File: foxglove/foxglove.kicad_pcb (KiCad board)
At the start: 4 copper layers, 70.7 x 53.3 mm, 106 parts, among them IC1 LFE5U-12F-6BG256C, J1 NEIGHBOR1, J2 NEIGHBOR2, J3 Conn_02x05_Odd_Even, J4 Conn_02x05_Odd_Even, J5 Conn_01x02_Female, J7 BONUS_ROW, U1 ICE40HX8K-CT256, U10 SHIFTER, U11 74HC4051, U12 SHIFTER, U13 74HC4051, U14 SHIFTER, U15 74HC4051, U16 SHIFTER, U17 74HC4051, U18 SHIFTER, U19 74HC4051, U2 ADP225, U20 SHIFTER, U21 74HC4051, U22 SHIFTER, U23 74HC4051, U24 SHIFTER, U3 MC4558CPT, U4 74LVC1G3157, U5 LM339, U6 ADP225, U7 DAC084S085, U8 74AHC1G04, U9 74HC4051

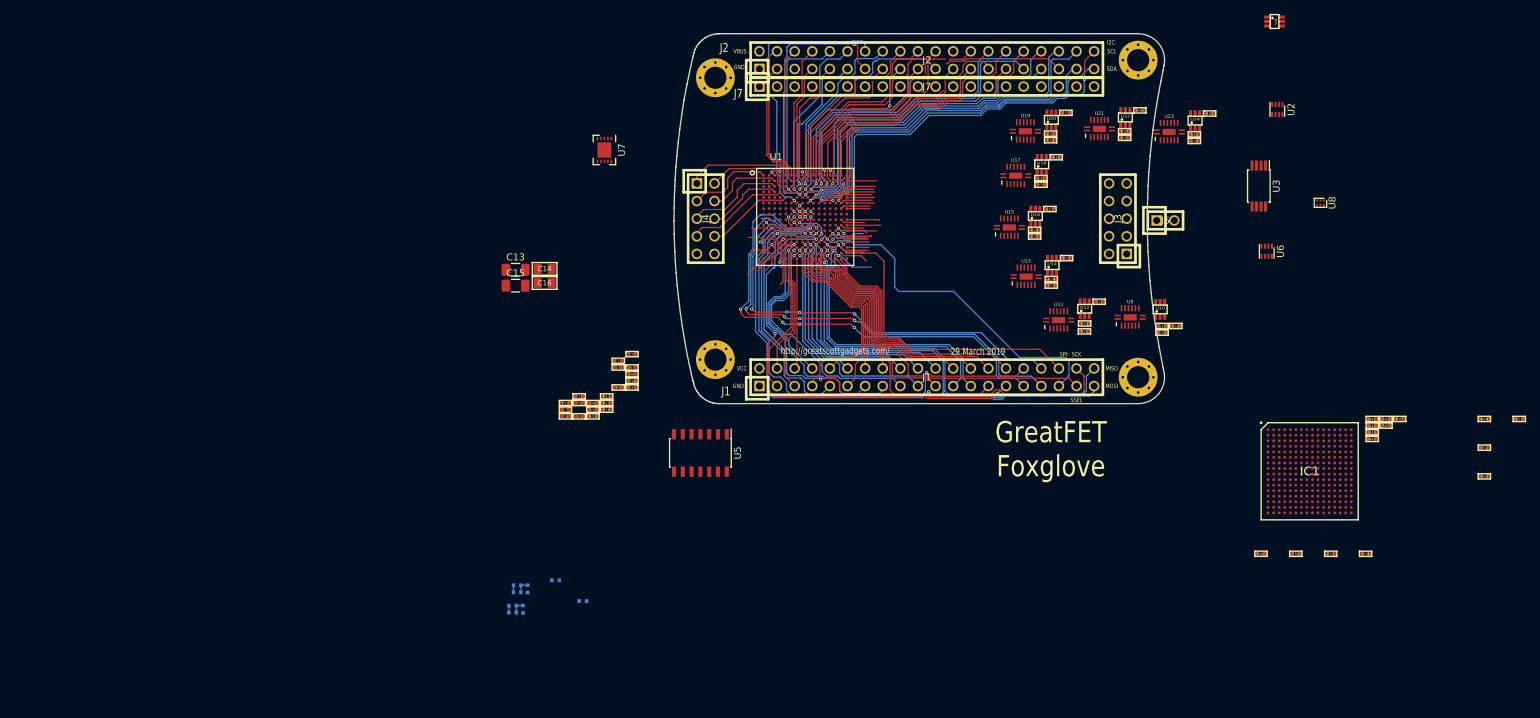
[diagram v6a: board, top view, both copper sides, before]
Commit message: Started routing connections to J2 and J7
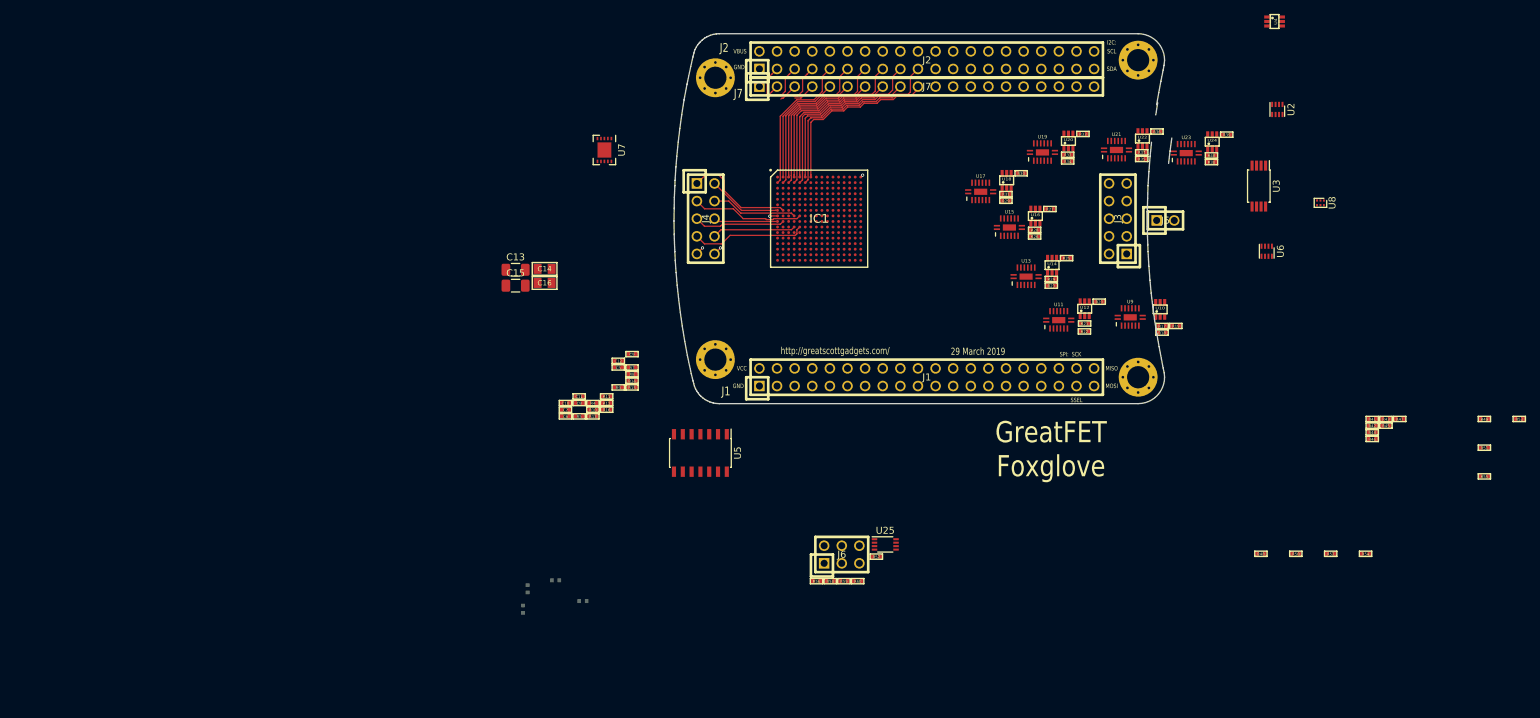
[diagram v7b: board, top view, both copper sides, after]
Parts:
- removed C1, C3: 10uF, gsg-modules:0402
- removed C2, C4: 100nF, gsg-modules:0402
- removed U1: ICE40HX8K-CT256, gsg-modules:BGA256C80P16X16_1400X1400X170
- added J6: Conn_02x03_Odd_Even, gsg-modules:HEADER-2x3, F.Cu at (133.8, 143.7)
- added R56: 4.7k, gsg-modules:0402, F.Cu at (130.1, 147.5)
- added R57: 4.7k, gsg-modules:0402, F.Cu at (138.8, 144.0)
- added R58: 1k, gsg-modules:0402, F.Cu at (132.1, 147.5)
- added R59: 4.7k, gsg-modules:0402, F.Cu at (134.1, 147.5)
- added R60: 4.7k, gsg-modules:0402, F.Cu at (136.1, 147.5)
- added U25: 74LVC1G53, Package_SO:VSSOP-8_2.3x2mm_P0.5mm, F.Cu at (140.1, 142.2)
- R1, R4, R5: value 10k -> 4.7k
- R2: value ??? -> 4.7k
- R3, R6: value 100 -> 4.7k
- moved IC1 79.6 mm to (130.5, 95.2)
- moved R30 5.56 mm to (159.7, 88.7)
- moved R31 5.56 mm to (157.5, 91.7)
- moved U18 5.56 mm to (157.6, 89.7)
- moved R29 5.56 mm to (157.5, 92.7)
- moved U17 5.56 mm to (153.8, 91.4)
- moved U21 3.92 mm to (173.4, 85.3)
- moved U22 3.92 mm to (177.2, 83.7)
- moved R32 3.92 mm to (166.4, 86.0)
- moved R33 3.92 mm to (168.6, 83.0)
- moved R35 3.92 mm to (177.0, 86.6)
- moved R36 3.92 mm to (179.2, 82.7)
- moved R37 3.92 mm to (177.0, 85.7)
- moved R38 3.92 mm to (187.1, 87.1)
- moved R39 3.92 mm to (189.3, 83.1)
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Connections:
- IC1 pad A10: (no net) -> /J7.13
- IC1 pad A11: (no net) -> /J7.14
- IC1 pad A12: (no net) -> /J7.15
- IC1 pad A13: (no net) -> /J7.16
- IC1 pad A14: (no net) -> /J7.17
- IC1 pad A15: (no net) -> /J7.18
- IC1 pad A2: (no net) -> /J7.05
- IC1 pad A3: (no net) -> /J7.06
- IC1 pad A4: (no net) -> /J7.07
- IC1 pad A5: (no net) -> /J7.08
- IC1 pad A6: (no net) -> /J7.09
- IC1 pad A7: (no net) -> /J7.10
- IC1 pad A8: (no net) -> /J7.11
- IC1 pad A9: (no net) -> /J7.12
- IC1 pad B1: (no net) -> /J2.09
- IC1 pad B10: (no net) -> /J2.27
- IC1 pad B11: (no net) -> /J2.29
- IC1 pad B12: (no net) -> /J2.31
- IC1 pad B13: (no net) -> /J2.33
- IC1 pad B14: (no net) -> /J2.35
- IC1 pad B15: (no net) -> /J2.37
- IC1 pad B16: (no net) -> /J2.39
- IC1 pad B2: (no net) -> /J2.11
- IC1 pad B3: (no net) -> /J2.13
- IC1 pad B4: (no net) -> /J2.15
- IC1 pad B5: (no net) -> /J2.17
- IC1 pad B6: (no net) -> /J2.19
- IC1 pad B7: (no net) -> /J2.21
- IC1 pad B8: (no net) -> /J2.23
- IC1 pad B9: (no net) -> /J2.25
- IC1 pad C1: (no net) -> /J2.10
- IC1 pad C10: (no net) -> /J2.28
- IC1 pad C11: (no net) -> /J2.30
- IC1 pad C12: (no net) -> /J2.32
- IC1 pad C13: (no net) -> /J2.34
- IC1 pad C14: (no net) -> /J2.36
- IC1 pad C15: (no net) -> /J2.38
- IC1 pad C16: (no net) -> /J2.40
- IC1 pad C2: (no net) -> /J2.12
- IC1 pad C3: (no net) -> /J2.14
- IC1 pad C4: (no net) -> /J2.16
- IC1 pad C5: (no net) -> /J2.18
- IC1 pad C6: (no net) -> /J2.20
- IC1 pad C7: (no net) -> /J2.22
- IC1 pad C8: (no net) -> /J2.24
- IC1 pad C9: (no net) -> /J2.26
- IC1 pad G1: (no net) -> /B2
- IC1 pad G2: (no net) -> /B1
- IC1 pad H4: (no net) -> /B4
- IC1 pad H5: (no net) -> /B3
- IC1 pad J1: (no net) -> /B6
- IC1 pad J2: (no net) -> /B5
- IC1 pad K4: (no net) -> /B8
- IC1 pad K5: (no net) -> /B7
- IC1 pad L6: (no net) -> VCC
- IC1 pad M10: (no net) -> /TDO
- IC1 pad N10: (no net) -> /CFG_0
- IC1 pad N8: (no net) -> /CSSPIN
- IC1 pad N9: (no net) -> /SCK
- IC1 pad P10: (no net) -> /CFG_1
- IC1 pad R1: (no net) -> /J1.13
- IC1 pad R10: (no net) -> /CFG_2
- IC1 pad R11: (no net) -> /TDI
- IC1 pad R12: (no net) -> /J1.27
- IC1 pad R13: (no net) -> /J1.29
- IC1 pad R14: (no net) -> /J1.31
- IC1 pad R15: (no net) -> /J1.33
- IC1 pad R16: (no net) -> /J1.35
- IC1 pad R2: (no net) -> /J1.15
- IC1 pad R3: (no net) -> /J1.17
- IC1 pad R4: (no net) -> /J1.19
- IC1 pad R5: (no net) -> /J1.21
- IC1 pad R6: (no net) -> /J1.23
- IC1 pad R7: (no net) -> /J1.25
- IC1 pad R8: (no net) -> /SSEL
- IC1 pad R9: (no net) -> /PROGRAMN
- IC1 pad T10: (no net) -> /TCK
- IC1 pad T11: (no net) -> /TMS
- IC1 pad T13: (no net) -> /J1.32
- IC1 pad T14: (no net) -> /J1.34
- IC1 pad T15: (no net) -> /J1.36
- IC1 pad T2: (no net) -> /J1.24
- IC1 pad T3: (no net) -> /J1.26
- IC1 pad T4: (no net) -> /J1.28
- IC1 pad T6: (no net) -> /J1.30
- IC1 pad T7: (no net) -> /MISO
- IC1 pad T8: (no net) -> /MOSI
- IC1 pad T9: (no net) -> /INITN
- J1 pad 10: /J1.10 -> (no net)
- J1 pad 11: /J1.11 -> (no net)
- J1 pad 12: /J1.12 -> (no net)
- J1 pad 14: /J1.14 -> (no net)
- J1 pad 16: /J1.16 -> (no net)
- J1 pad 18: /J1.18 -> (no net)
- J1 pad 20: /J1.20 -> (no net)
- J1 pad 22: /J1.22 -> (no net)
- J1 pad 3: /J1.03 -> (no net)
- J1 pad 4: /J1.04 -> (no net)
- J1 pad 5: /J1.05 -> (no net)
- J1 pad 6: /J1.06 -> (no net)
- J1 pad 7: /J1.07 -> (no net)
- J1 pad 8: /J1.08 -> (no net)
- J1 pad 9: /J1.09 -> (no net)
- J2 pad 3: /J2.03 -> (no net)
- J2 pad 4: /J2.04 -> (no net)
- J2 pad 6: /J2.06 -> (no net)
- J2 pad 7: /J2.07 -> (no net)
- J2 pad 8: /J2.08 -> (no net)
- J7 pad 1: (no net) -> GND
- J7 pad 10: (no net) -> /J7.10
- J7 pad 11: (no net) -> /J7.11
- J7 pad 12: (no net) -> /J7.12
- J7 pad 13: (no net) -> /J7.13
- J7 pad 14: (no net) -> /J7.14
- J7 pad 15: (no net) -> /J7.15
- J7 pad 16: (no net) -> /J7.16
- J7 pad 17: (no net) -> /J7.17
- J7 pad 18: (no net) -> /J7.18
- J7 pad 19: (no net) -> GND
- J7 pad 20: (no net) -> VCC
- J7 pad 5: (no net) -> /J7.05
- J7 pad 6: (no net) -> /J7.06
- J7 pad 7: (no net) -> /J7.07
- J7 pad 8: (no net) -> /J7.08
- J7 pad 9: (no net) -> /J7.09
- R1 pad 2: /CRESET -> /TMS
- R2 pad 2: /CDONE -> /TCK
- R3 pad 1: +1V2 -> VCC
- R3 pad 2: Net-(C1-Pad2) -> /INITN
- R4 pad 2: /SCK -> /TDI
- R45 pad 1: (no net) -> /EN_pull
- R46 pad 2: (no net) -> Net-(R46-Pad2)
- R47 pad 1: (no net) -> Net-(R47-Pad1)
- R5 pad 2: /SSEL -> /CFG_2
- R6 pad 1: +1V2 -> VCC
- R6 pad 2: Net-(C3-Pad2) -> /PROGRAMN
- U10 pad 3: /A1_shift -> (no net)
- U10 pad 5: /DIR_1 -> (no net)
- U11 pad 10: /S1_2 -> (no net)
- U11 pad 11: /S0_2 -> (no net)
- U11 pad 9: /S2_2 -> (no net)
- U12 pad 3: /A2_shift -> (no net)
- U12 pad 5: /DIR_2 -> (no net)
- U13 pad 10: /S1_3 -> (no net)
- U13 pad 11: /S0_3 -> (no net)
- U13 pad 9: /S2_3 -> (no net)
- U14 pad 3: /A3_shift -> (no net)
- U14 pad 5: /DIR_3 -> (no net)
- U15 pad 10: /S1_4 -> (no net)
- U15 pad 11: /S0_4 -> (no net)
- U15 pad 9: /S2_4 -> (no net)
- U16 pad 3: /A4_shift -> (no net)
- U16 pad 5: /DIR_4 -> (no net)
- U17 pad 10: /S1_5 -> (no net)
- U17 pad 11: /S0_5 -> (no net)
- U17 pad 9: /S2_5 -> (no net)
- U18 pad 3: /A5_shift -> (no net)
- U18 pad 5: /DIR_5 -> (no net)
- U19 pad 10: /S1_6 -> (no net)
- U19 pad 11: /S0_6 -> (no net)
- U19 pad 9: /S2_6 -> (no net)
- U20 pad 3: /A6_shift -> (no net)
- U20 pad 5: /DIR_6 -> (no net)
- U21 pad 10: /S1_7 -> (no net)
- U21 pad 11: /S0_7 -> (no net)
- U21 pad 9: /S2_7 -> (no net)
- U22 pad 3: /A7_shift -> (no net)
- U22 pad 5: /DIR_7 -> (no net)
- U23 pad 10: /S1_8 -> (no net)
- U23 pad 11: /S0_8 -> (no net)
- U23 pad 9: /S2_8 -> (no net)
- U24 pad 3: /A8_shift -> (no net)
- U24 pad 5: /DIR_8 -> (no net)
- U5 pad 1: /COUT1 -> (no net)
- U5 pad 13: /COUT4 -> (no net)
- U5 pad 14: /COUT3 -> (no net)
- U5 pad 2: /COUT2 -> (no net)
- U6 pad 1: /VCCA_EN -> (no net)
- U6 pad 2: /DAC2_EN -> (no net)
- U9 pad 10: /S1_1 -> (no net)
- U9 pad 11: /S0_1 -> (no net)
- U9 pad 9: /S2_1 -> (no net)
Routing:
- net /J1.31: track 73.6 -> 0.00 mm, vias 5 -> 0
- net /J1.33: track 72.6 -> 0.00 mm, vias 5 -> 0
- net /J1.32: track 70.6 -> 0.00 mm, vias 2 -> 0
- net /J1.34: track 65.7 -> 0.00 mm, vias 5 -> 0
- net /J1.27: track 64.1 -> 0.00 mm, vias 2 -> 0
- net /J1.29: track 63.3 -> 0.00 mm, vias 3 -> 0
- net /MISO: track 62.2 -> 0.00 mm, vias 1 -> 0
- net /MOSI: track 60.5 -> 0.00 mm, vias 1 -> 0
- net /SCK: track 59.9 -> 0.00 mm
- net /J2.38: track 55.6 -> 0.00 mm, vias 1 -> 0
- net /J2.40: track 55.5 -> 0.00 mm, vias 2 -> 0
- net /J2.39: track 54.7 -> 0.00 mm, vias 1 -> 0
- net /J2.37: track 51.5 -> 0.00 mm, vias 1 -> 0
- net /SSEL: track 51.2 -> 0.00 mm
- net /J2.36: track 50.4 -> 0.00 mm, vias 1 -> 0
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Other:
- board size 70.7 x 53.3 mm -> 71.8 x 53.3 mm

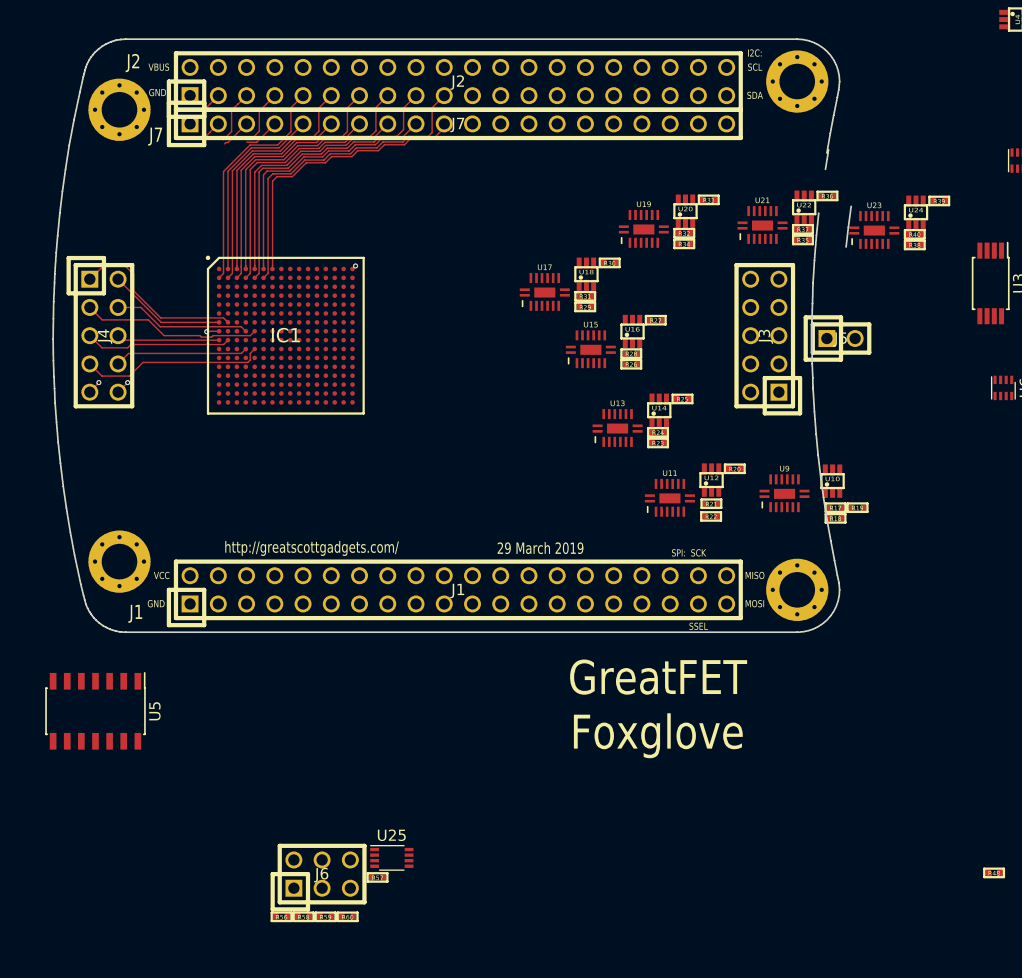
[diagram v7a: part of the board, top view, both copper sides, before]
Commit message: Routed all greatfet headers to FPGA
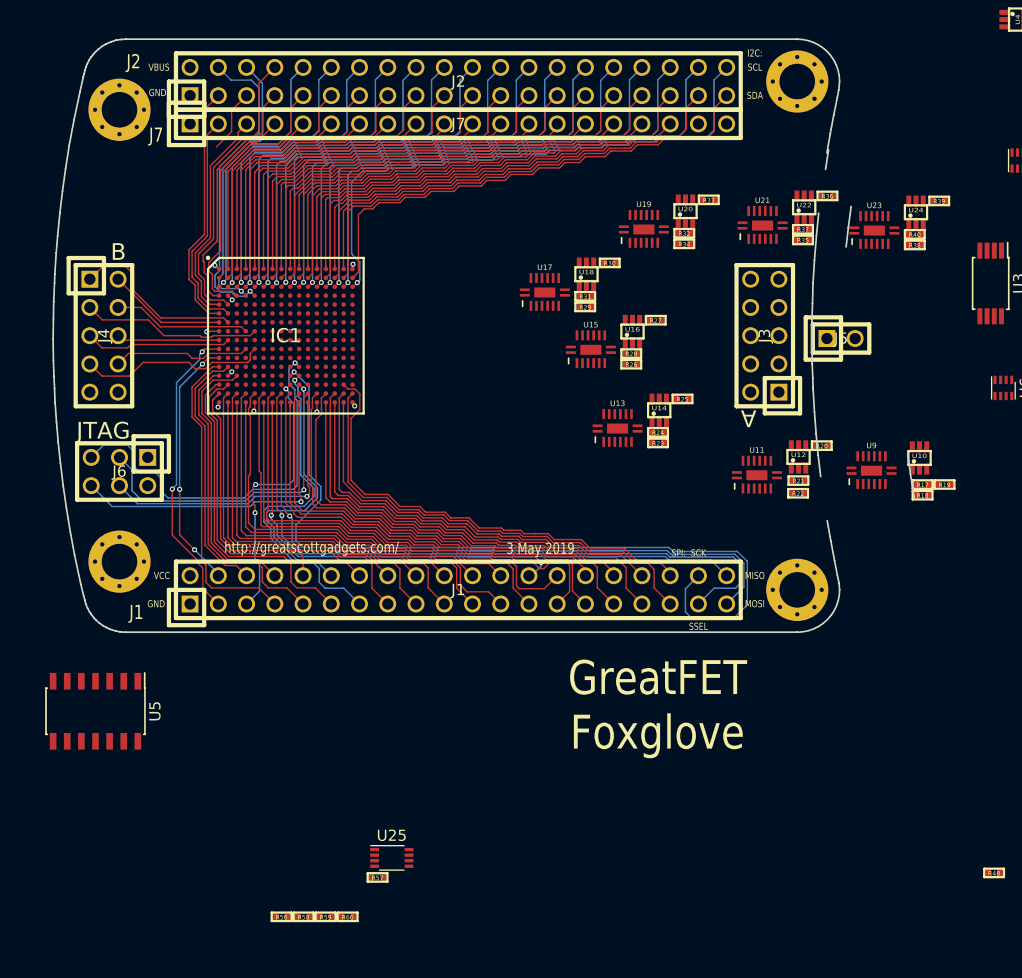
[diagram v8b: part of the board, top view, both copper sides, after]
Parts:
- moved J6 40.5 mm to (115.6, 107.5), turned to 180 degrees
- moved R19 8.10 mm to (189.8, 108.6)
- moved R20 8.10 mm to (178.7, 105.1)
- moved R22 8.10 mm to (176.6, 109.4)
- moved R17 8.10 mm to (187.8, 108.6)
- moved R18 8.10 mm to (187.8, 109.6)
- moved R21 8.10 mm to (176.6, 108.3)
- moved U10 8.10 mm to (187.5, 106.2)
- moved U12 8.10 mm to (176.6, 106.2)
- moved U9 8.10 mm to (183.2, 107.4)
- moved U11 8.10 mm to (172.9, 107.8)
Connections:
- IC1 pad D1: (no net) -> /J2.07
- IC1 pad D3: (no net) -> /J7.04
- IC1 pad D4: (no net) -> /J2.06
- IC1 pad D5: (no net) -> /J2.04
- IC1 pad E1: (no net) -> /J7.03
- IC1 pad E2: (no net) -> /J2.08
- IC1 pad F1: (no net) -> /J2.03
- IC1 pad F2: (no net) -> /J7.02
- IC1 pad K1: (no net) -> /J1.03
- IC1 pad L1: (no net) -> /J1.04
- IC1 pad M1: (no net) -> /J1.07
- IC1 pad M2: (no net) -> /J1.06
- IC1 pad N1: (no net) -> /J1.09
- IC1 pad N3: (no net) -> /J1.08
- IC1 pad P1: (no net) -> /J1.11
- IC1 pad P15: (no net) -> /J1.36
- IC1 pad P2: (no net) -> /J1.10
- IC1 pad P9: (no net) -> /DONE
- IC1 pad R1: /J1.13 -> /J1.14
- IC1 pad R12: /J1.27 -> /J1.26
- IC1 pad R7: /J1.25 -> /J1.24
- IC1 pad T13: /J1.32 -> /J1.30
- IC1 pad T14: /J1.34 -> /J1.32
- IC1 pad T15: /J1.36 -> /J1.34
- IC1 pad T2: /J1.24 -> /J1.16
- IC1 pad T3: /J1.26 -> /J1.18
- IC1 pad T4: /J1.28 -> /J1.20
- IC1 pad T6: /J1.30 -> /J1.22
- J1 pad 10: (no net) -> /J1.10
- J1 pad 11: (no net) -> /J1.11
- J1 pad 12: (no net) -> /CFG_1
- J1 pad 13: /J1.13 -> /CFG_0
- J1 pad 14: (no net) -> /J1.14
- J1 pad 16: (no net) -> /J1.16
- J1 pad 18: (no net) -> /J1.18
- J1 pad 20: (no net) -> /J1.20
- J1 pad 22: (no net) -> /J1.22
- J1 pad 25: /J1.25 -> /PROGRAMN
- J1 pad 27: /J1.27 -> /CFG_2
- J1 pad 28: /J1.28 -> /INITN
- J1 pad 3: (no net) -> /J1.03
- J1 pad 4: (no net) -> /J1.04
- J1 pad 5: (no net) -> /DONE
- J1 pad 6: (no net) -> /J1.06
- J1 pad 7: (no net) -> /J1.07
- J1 pad 8: (no net) -> /J1.08
- J1 pad 9: (no net) -> /J1.09
- J2 pad 3: (no net) -> /J2.03
- J2 pad 4: (no net) -> /J2.04
- J2 pad 6: (no net) -> /J2.06
- J2 pad 7: (no net) -> /J2.07
- J2 pad 8: (no net) -> /J2.08
- J7 pad 2: (no net) -> /J7.02
- J7 pad 3: (no net) -> /J7.03
- J7 pad 4: (no net) -> /J7.04
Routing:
- net /SCK: track 0.00 -> 72.8 mm, vias 0 -> 1
- net /SSEL: track 0.00 -> 61.8 mm, vias 0 -> 1
- net /MOSI: track 0.00 -> 58.7 mm, vias 0 -> 1
- net /MISO: track 0.00 -> 54.2 mm, vias 0 -> 1
- net /J2.40: track 0.00 -> 50.6 mm, vias 0 -> 1
- net /J2.38: track 0.00 -> 48.4 mm, vias 0 -> 1
- net /J2.36: track 0.00 -> 46.9 mm, vias 0 -> 1
- net /J2.34: track 0.00 -> 45.3 mm, vias 0 -> 1
- net /J2.39: track 0.00 -> 44.7 mm
- net /J2.32: track 0.00 -> 43.5 mm, vias 0 -> 1
- net /J2.37: track 0.00 -> 43.1 mm
- net /J1.35: track 0.00 -> 42.6 mm
- net /J1.36: track 0.00 -> 42.3 mm
- net /J2.30: track 0.00 -> 41.9 mm, vias 0 -> 1
- net /CFG_2: track 0.00 -> 41.4 mm
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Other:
- board size 71.8 x 53.3 mm -> 77.4 x 53.3 mm
- board text added: "3 May 2019"
- board text added: "A"
- board text added: "B"
- board text added: "JTAG"
- board text removed: "29 March 2019"
